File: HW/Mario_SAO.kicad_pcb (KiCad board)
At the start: 0 parts

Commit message: Adding netlist and edge.cuts to PCB
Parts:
- added D1: LED, Mario_SAO:1204_SIDE_VIEW_LED, F.Cu at (94.8, 88.6)
- added D2: LED, Mario_SAO:1204_SIDE_VIEW_LED, F.Cu at (94.8, 92.7)
- added D3: LED, Mario_SAO:1204_SIDE_VIEW_LED, F.Cu at (100.1, 88.6)
- added D4: LED, Mario_SAO:1204_SIDE_VIEW_LED, F.Cu at (94.8, 96.7)
- added R1: 50R, Resistor_SMD:R_0805_2012Metric_Pad1.15x1.40mm_HandSolder, F.Cu at (78.1, 101.3)
- added R2: 50R, Resistor_SMD:R_0805_2012Metric_Pad1.15x1.40mm_HandSolder, F.Cu at (99.8, 92.0)
- added X1: Badgelife_sao_connector_v169bis, Mario_SAO:Badgelife-SAOv169-SAO-2x3, F.Cu at (84.0, 94.7)
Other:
- copper layers 0 -> 2
- net class Default added: clearance 0.2, trace_width 0.25, via_dia 0.8, via_drill 0.4

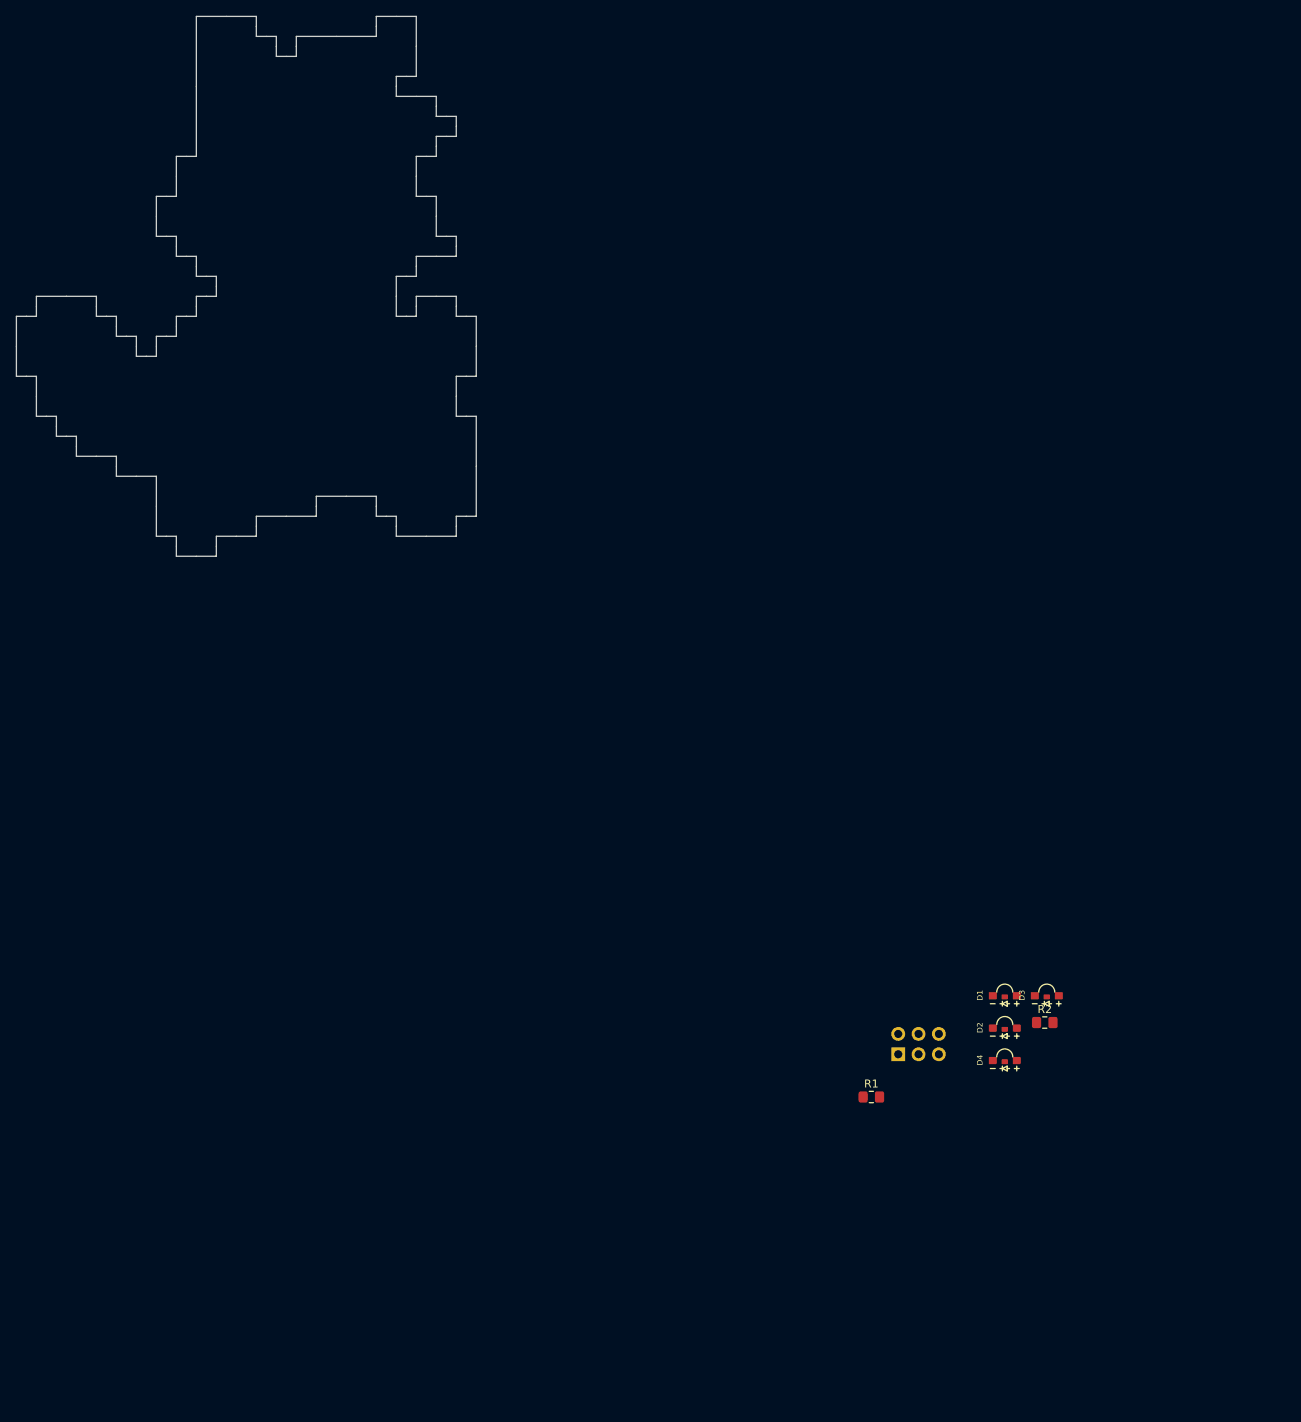
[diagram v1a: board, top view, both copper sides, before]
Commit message: placeing LEDs
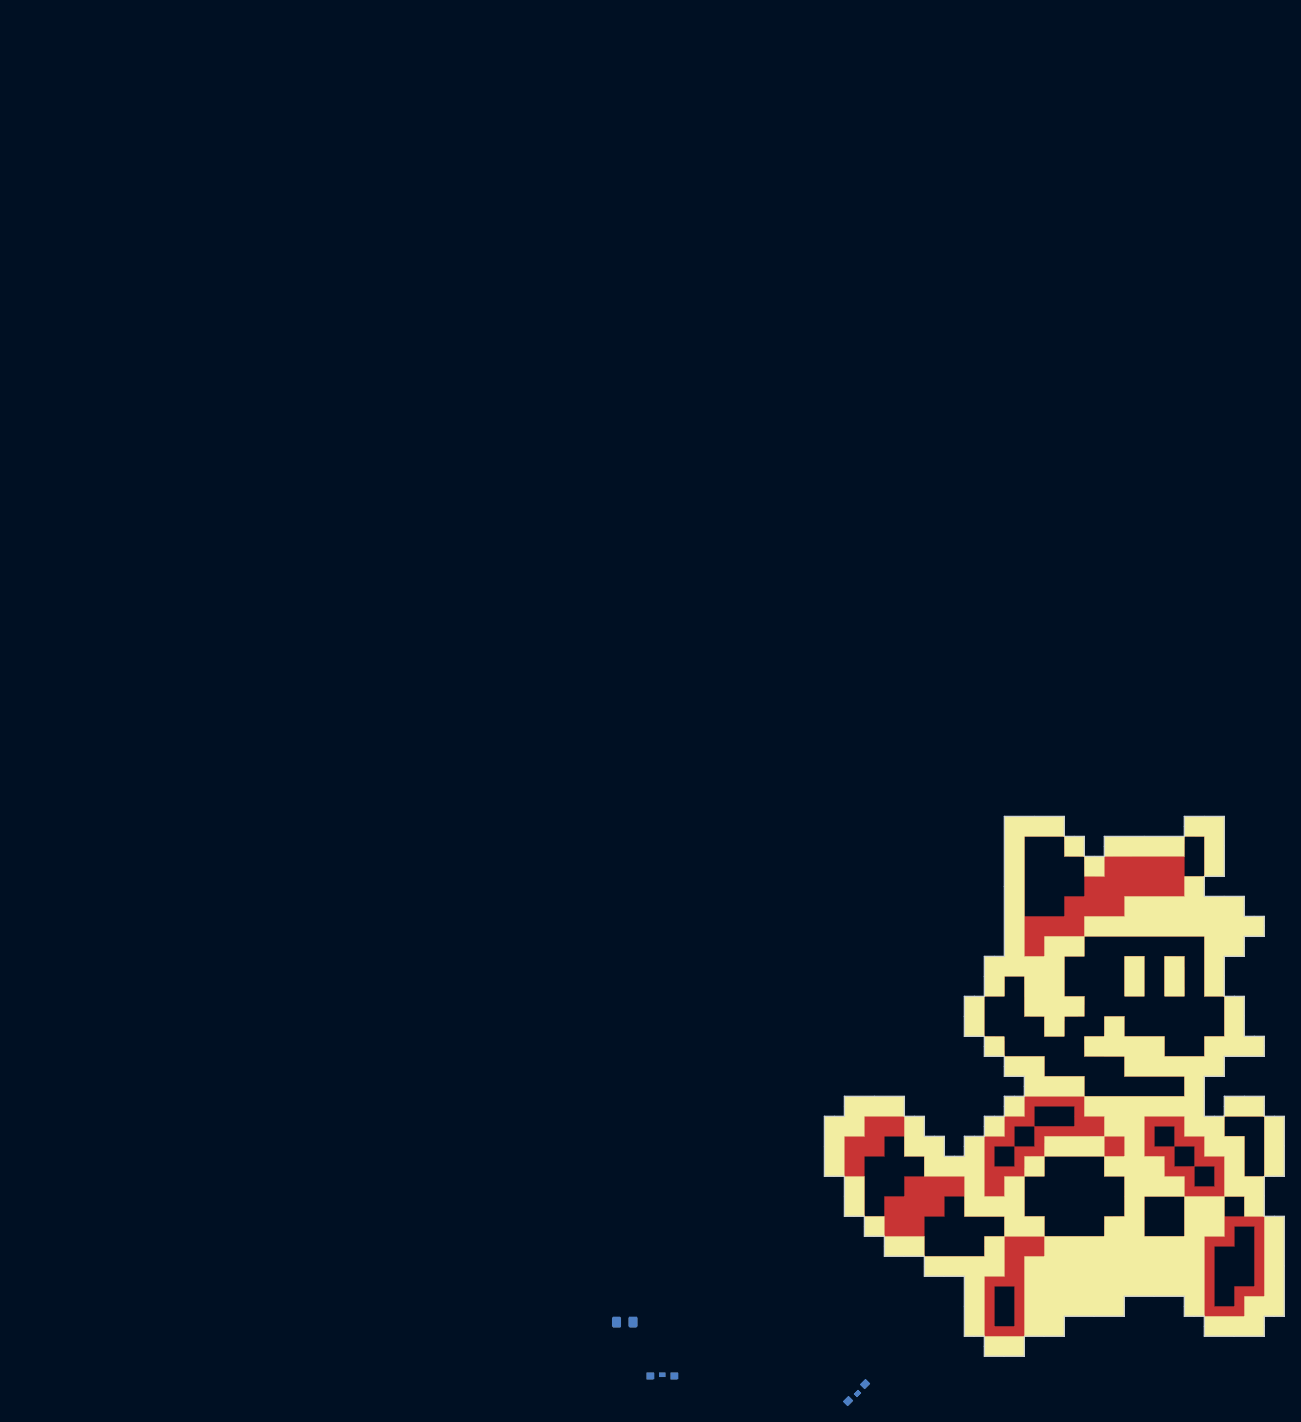
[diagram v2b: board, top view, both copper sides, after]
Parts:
- added G***: LOGO, Mario_SAO:F.Silk_g4158, F.Cu at (101.0, 100.0)
- added G***: LOGO, Mario_SAO:F.Mask_g4156, F.Cu at (101.0, 100.0)
- added G***: LOGO, Mario_SAO:B.Mask_g4150, F.Cu at (101.0, 100.0)
- added G***: LOGO, Mario_SAO:F.Cu_g4154, F.Cu at (101.0, 100.0)
- D1, D2, D3, D4, R1, R2: moved to B.Cu
- moved D3 67.7 mm to (52.0, 136.2)
- moved R2 64.5 mm to (47.3, 129.5)
- moved D4 45.5 mm to (76.2, 138.2), turned to 225 degrees
- moved X1 36.3 mm to (108.8, 121.2)
- moved D1 34.6 mm to (94.8, 123.2)
- moved R1 25.5 mm to (96.8, 118.8), turned to 270 degrees
- moved D2 15.6 mm to (99.8, 107.5), turned to 225 degrees

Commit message: Adding trace and B.Cu keepout
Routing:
- net VCC: track 0.00 -> 10.5 mm
- net Net-(D1-Pad2): track 0.00 -> 3.63 mm
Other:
- net class Default: clearance 0.2 -> 0.1524; trace_width 0.25 -> 0.1524
- rule trace_clearance: 0.2 -> 0.1524
- rule trace_min: 0.2 -> 0.1524
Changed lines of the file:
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@@
     (thickness 1.6)
     (drawings 183)
-    (tracks 0)
+    (tracks 4)
     (zones 0)
     (modules 11)
@@
   )
   (setup
-    (last_trace_width 0.25)
-    (trace_clearance 0.2)
+    (last_trace_width 0.254)
+    (user_trace_width 0.1524)
+    (user_trace_width 0.2032)
+    (user_trace_width 0.254)
+    (trace_clearance 0.1524)
     (zone_clearance 0.508)
     (zone_45_only no)
-    (trace_min 0.2)
+    (trace_min 0.1524)
     (via_size 0.8)
     (via_drill 0.4)
@@
   (net 8 "Net-(X1-Pad4)")
   (net_class Default "This is the default net class."
-    (clearance 0.2)
-    (trace_width 0.25)
+    (clearance 0.1524)
+    (trace_width 0.1524)
     (via_dia 0.8)
     (via_drill 0.4)
@@
   (gr_line (start 92.252684 132.491508) (end 92.252684 132.491508) (layer Edge.Cuts) (width 0.1))
   (gr_line (start 92.252684 132.491508) (end 92.252684 132.491508) (layer Edge.Cuts) (width 0.1))
+  (segment (start 96.25 120.275) (end 96.75 119.775) (width 0.254) (layer B.Cu) (net 1))
+  (segment (start 96.25 123.2) (end 96.25 120.275) (width 0.254) (layer B.Cu) (net 1))
+  (segment (start 99.025 120) (end 96.75 117.725) (width 0.254) (layer B.Cu) (net 4))
+  (segment (start 106.27 120) (end 99.025 120) (width 0.254) (layer B.Cu) (net 4))
+  (zone (net 0) (net_name "") (layer B.Cu) (hatch full 0.508)
+    (connect_pads (clearance 0.508))
+    (min_thickness 0.254)
+    (keepout (tracks not_allowed) (vias not_allowed) (copperpour not_allowed))
+    (fill (arc_segments 32) (thermal_gap 0.508) (thermal_bridge_width 0.508))
+    (polygon
+      (pts
+        (xy 96 130) (xy 96 125) (xy 93.5 125) (xy 93.5 130)
+      )
+    )
+  )
 )
